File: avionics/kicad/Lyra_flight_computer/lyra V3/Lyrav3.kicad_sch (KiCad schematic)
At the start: 84 parts, among them J1 Screw_Terminal_01x08, J2 Screw_Terminal_01x06, J3 Conn_01x02, J4 Conn_01x02, J5 Conn_01x03, J6 Conn_01x06, J7 USB_B_Micro, J8 Conn_01x04, Q1 AO3401A, Q2 KY6802, Q3 KY6802, U2 BMI088, U3 MPL3115A2, U4 ADXL375BCCZ-RL7, U5 LIS3MDL, U6 ADS1015IDGS, U7 W25Q64JVXGIQ, U8 RP2040, U9 LDK130-33_SOT23_SOT353, X1 S3D12.288000B20F30T

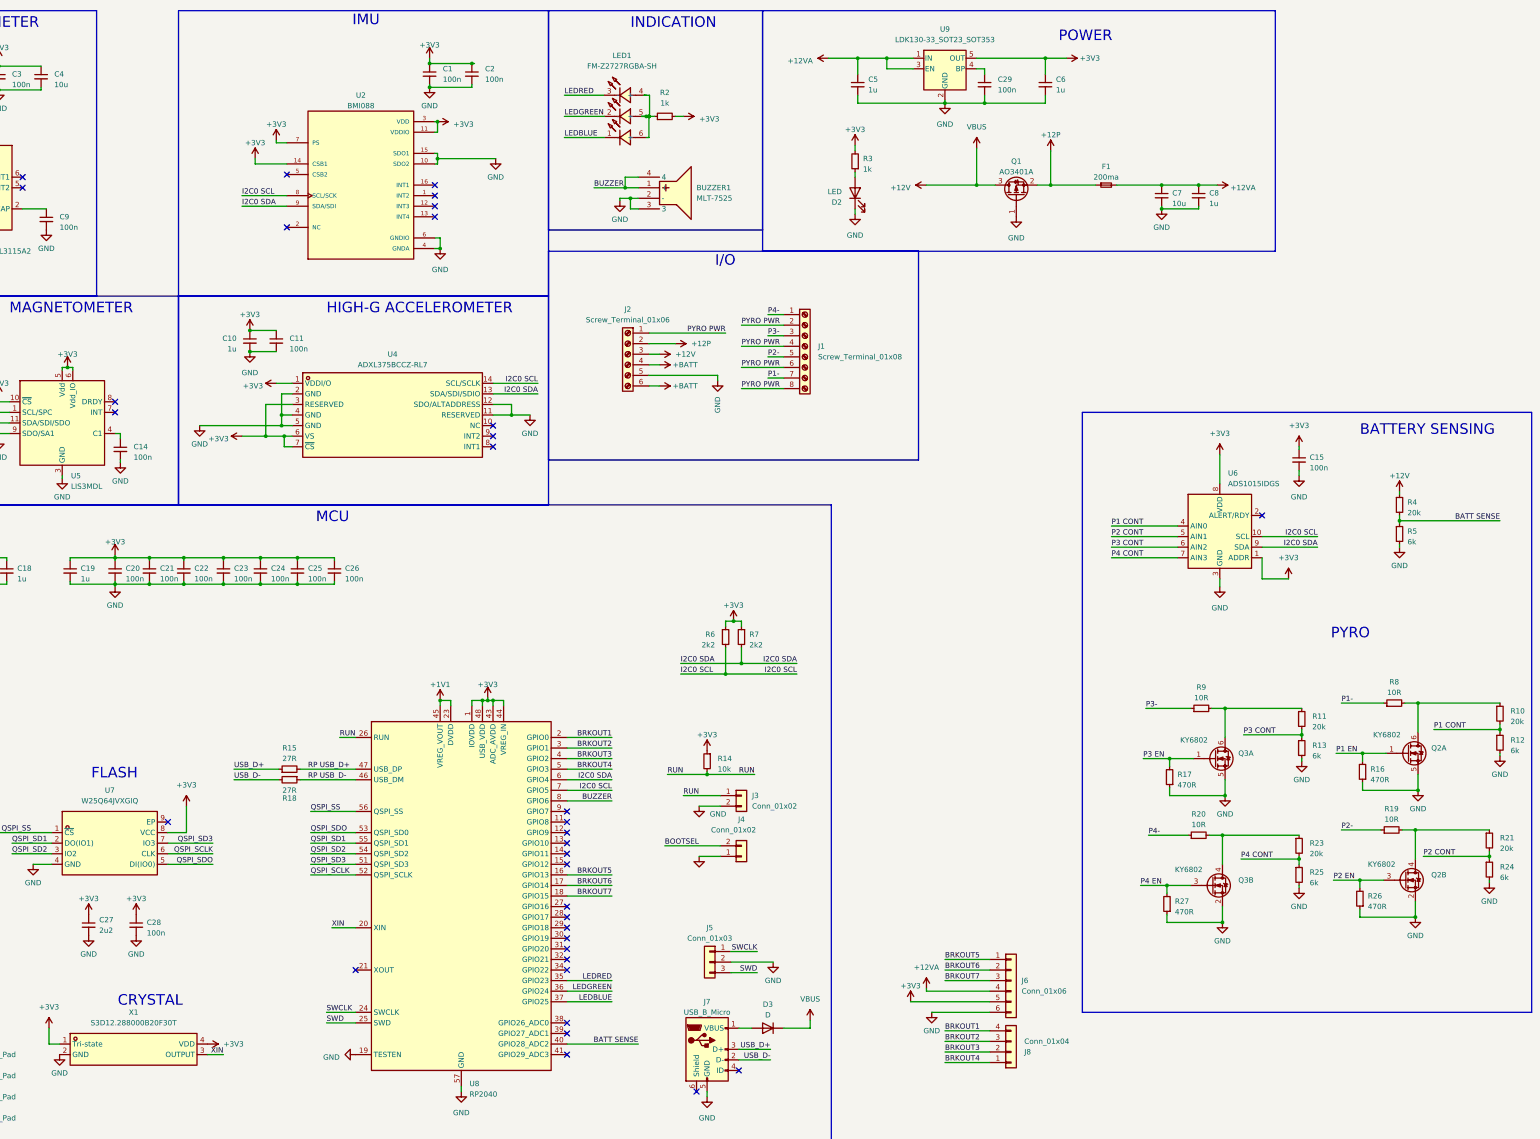
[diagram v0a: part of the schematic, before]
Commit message: more everything to back of board, find JLC components for everything
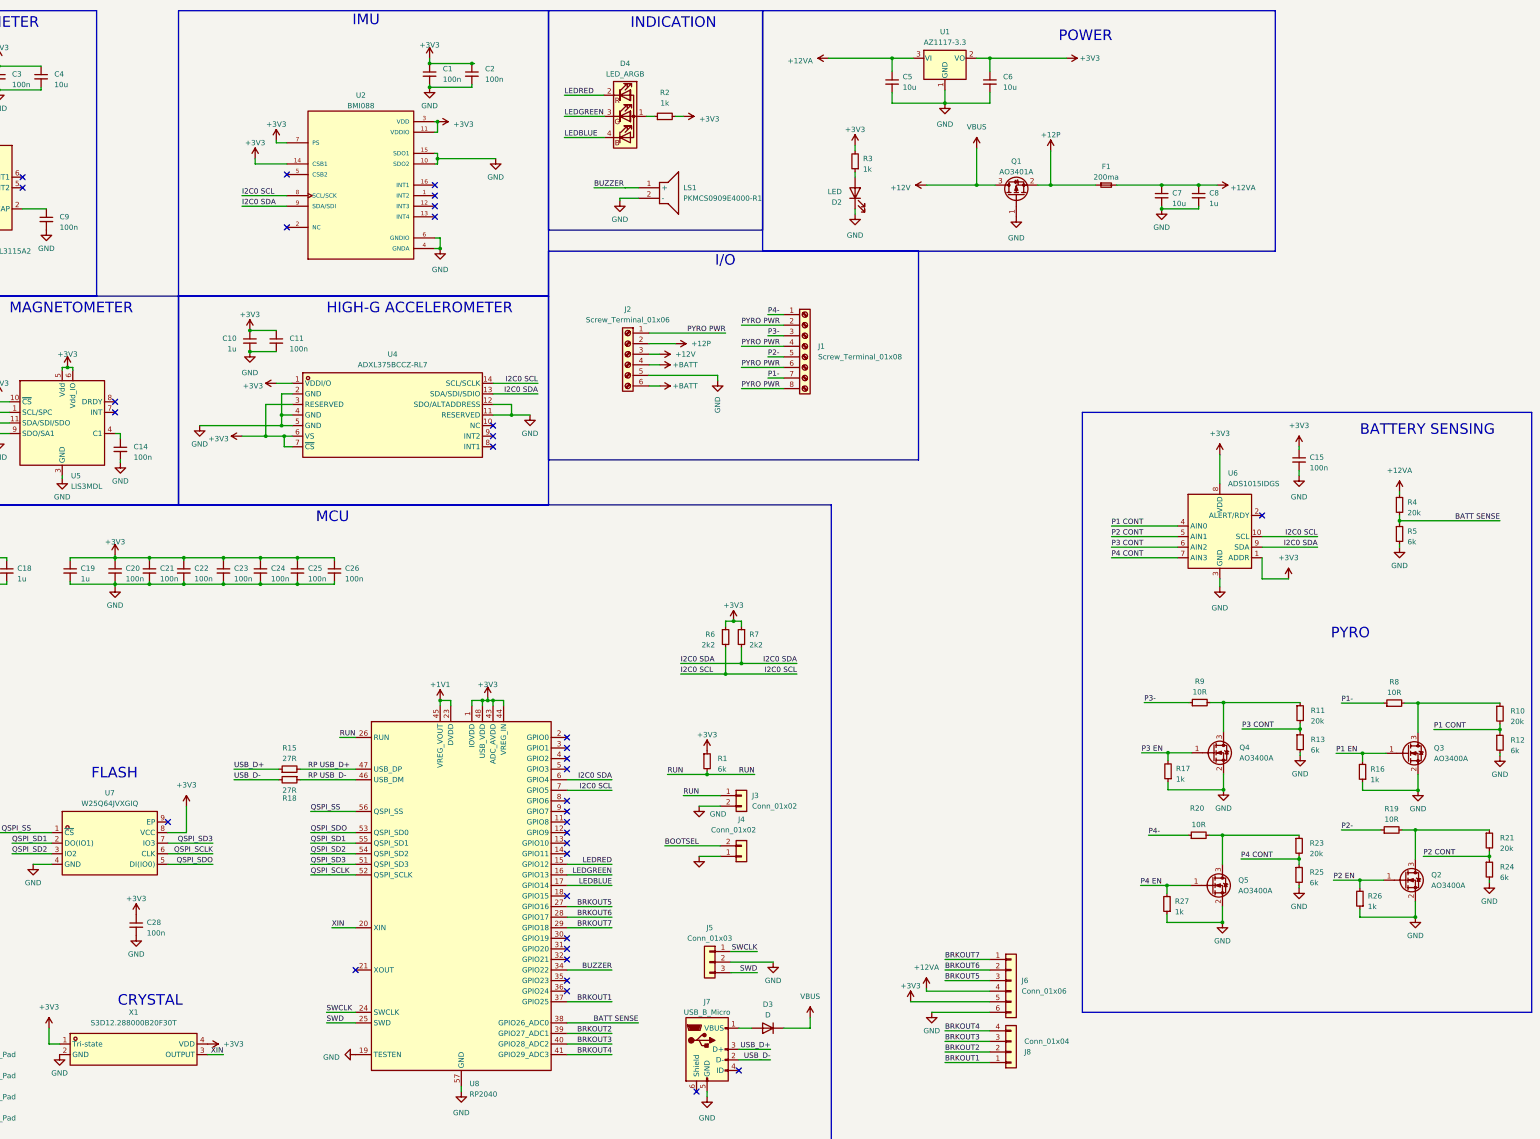
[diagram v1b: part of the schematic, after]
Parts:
- removed BUZZER1: MLT-7525, easyeda2kicad:BUZ-SMD_4P-L7.5-W7.5-P7.59-TL, symbol easyeda2kicad:MLT-7525
- removed C27: 2u2, Capacitor_SMD:C_0402_1005Metric, symbol Device:C_Small
- removed C29: 100n, Capacitor_SMD:C_0402_1005Metric, symbol Device:C_Small
- removed LED1: FM-Z2727RGBA-SH, easyeda2kicad:LED-SMD_6P-L2.7-W2.8-TL, symbol easyeda2kicad:FM-Z2727RGBA-SH
- removed Q2, Q3: KY6802, easyeda2kicad:SOT-23-6_L2.9-W1.6-P0.95-LS2.8-BL, symbol Device:Q_Dual_NMOS_G1S2G2D2S1D1
- removed R14: 10k, Resistor_SMD:R_0402_1005Metric, symbol Device:R_Small
- removed U9: LDK130-33_SOT23_SOT353, easyeda2kicad:SOT-23-5_L3.0-W1.6-P0.95-LS2.8-BL, symbol Regulator_Linear:LDK130-33_SOT23_SOT353
- added D4: LED_ARGB, customfootprints:LED_Cree-PLCC4_2x2mm_CCW, symbol Device:LED_ARGB
- added LS1: PKMCS0909E4000-R1, SamacSys_Parts4:PKMCS0909E4000R1, symbol SamacSys_Parts2:PKMCS0909E4000-R1
- added Q2, Q3, Q4, Q5: AO3400A, Package_TO_SOT_SMD:SOT-23, symbol Transistor_FET:AO3400A
- added R1: 6k, Resistor_SMD:R_0603_1608Metric, symbol Device:R_Small
- added U1: AZ1117-3.3, Package_TO_SOT_SMD:SOT-223, symbol Regulator_Linear:AZ1117-3.3
- C1, C11, C13, C14, C15, C16, C17, C2, C20, C21, C22, C23, C24, C25, C26, C28, C3, C9: footprint Capacitor_SMD:C_0402_1005Metric -> Capacitor_SMD:C_0603_1608Metric; LCSC Part (none) -> C14663
- C10, C12, C18, C19, C8: footprint Capacitor_SMD:C_0402_1005Metric -> Capacitor_SMD:C_0603_1608Metric; LCSC Part (none) -> C15849
- C4, C7: LCSC Part (none) -> C19702
- C5, C6: value 1u -> 10u; footprint Capacitor_SMD:C_0402_1005Metric -> Capacitor_SMD:C_0603_1608Metric; LCSC Part (none) -> C19702
- D2: LCSC Part (none) -> C2297
- D3: footprint Diode_SMD:D_0402_1005Metric -> Diode_SMD:D_SOD-323; LCSC Part (none) -> C2128
- F1: LCSC Part C883104 -> (none); now left out of the parts list
- H1, H2, H3, H4, J1, J2, J3, J6, J8: now left out of the parts list
- Q1: LCSC Part C306862 -> C15127
- R10, R11, R21, R23, R4: footprint Resistor_SMD:R_0402_1005Metric -> Resistor_SMD:R_0603_1608Metric; LCSC Part (none) -> C25804
- R12, R13, R24, R25, R5: footprint Resistor_SMD:R_0402_1005Metric -> Resistor_SMD:R_0603_1608Metric; LCSC Part (none) -> C4260
- R15, R18: footprint Resistor_SMD:R_0402_1005Metric -> Resistor_SMD:R_0603_1608Metric; LCSC Part C2909343 -> C25190
- R16, R17, R26, R27: value 470R -> 1k; footprint Resistor_SMD:R_0402_1005Metric -> Resistor_SMD:R_0603_1608Metric; LCSC Part (none) -> C21190
- R19, R20, R8, R9: footprint Resistor_SMD:R_0402_1005Metric -> Resistor_SMD:R_0603_1608Metric; LCSC Part (none) -> C22859
- R2, R22, R3: footprint Resistor_SMD:R_0402_1005Metric -> Resistor_SMD:R_0603_1608Metric; LCSC Part (none) -> C21190
- R6, R7: footprint Resistor_SMD:R_0402_1005Metric -> Resistor_SMD:R_0603_1608Metric; LCSC Part C163447 -> C4190
- U7: value W25Q64JVXGIQ -> W25Q64JVXGIQ; footprint easyeda2kicad:XSON-8_L4.0-W4.0-P0.80-TL-EP -> Package_SO:SOIC-8_5.23x5.23mm_P1.27mm; LCSC Part C2940195 -> C97521
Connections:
- net +12V: no longer R4.1
- net +12VA: now also R4.1, U1.3 (VI)
- net +3V3: now also R1.1, U1.2 (VO)
- net BATT SENSE : now also U8.38 (GPIO26_ADC0); no longer U8.40 (GPIO28_ADC2)
- net BRKOUT1: now also J8.1 (Pin_1), U8.37 (GPIO25); no longer J8.4 (Pin_4), U8.2 (GPIO0)
- net BRKOUT2: now also J8.2 (Pin_2), U8.39 (GPIO27_ADC1); no longer J8.3 (Pin_3), U8.3 (GPIO1)
- net BRKOUT3: now also J8.3 (Pin_3), U8.40 (GPIO28_ADC2); no longer J8.2 (Pin_2), U8.4 (GPIO2)
- net BRKOUT4: now also J8.4 (Pin_4), U8.41 (GPIO29_ADC3); no longer J8.1 (Pin_1), U8.5 (GPIO3)
- net BRKOUT5: now also J6.3 (Pin_3), U8.27 (GPIO16); no longer J6.1 (Pin_1), U8.16 (GPIO13)
- net BRKOUT6: now also U8.28 (GPIO17); no longer U8.17 (GPIO14)
- net BRKOUT7: now also J6.1 (Pin_1), U8.29 (GPIO18); no longer J6.3 (Pin_3), U8.18 (GPIO15)
- net BUZZER: now also U8.34 (GPIO22), LS1.1 (+); no longer U8.8 (GPIO6)
- net GND: now also LS1.2 (-), Q2.2 (S), Q3.2 (S), Q4.2 (S), Q5.2 (S), U1.1 (GND)
- net LEDBLUE: now also U8.17 (GPIO14), D4.4 (BK); no longer U8.37 (GPIO25)
- net LEDGREEN: now also U8.16 (GPIO13), D4.3 (GK); no longer U8.36 (GPIO24)
- net LEDRED: now also U8.15 (GPIO12), D4.2 (RK); no longer U8.35 (GPIO23)
- net P1 EN : now also Q3.1 (G)
- net P2 EN : now also Q2.1 (G)
- net P3 EN : now also Q4.1 (G)
- net P4 EN : now also Q5.1 (G)
- net RUN: now also R1.2
- net at R19.2, R21.1: now also Q2.3 (D)
- net at R11.1, R9.2: now also Q4.3 (D)
- net at R20.2, R23.1: now also Q5.3 (D)
- net at R10.1, R8.2: now also Q3.3 (D)
- net at R2.1: now also D4.1 (A)
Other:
- moved on the sheet: C5, C6, R11, R13, R17, R9

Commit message: routing init
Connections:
- net BUZZER: now also U8.32 (GPIO21); no longer U8.34 (GPIO22)
- net P1 EN : now also U8.6 (GPIO4)
- net P2 EN : now also U8.7 (GPIO5)
- net P3 EN : now also U8.8 (GPIO6)
- net P4 EN : now also U8.9 (GPIO7)
- net I2C1 SCL: now reaches U8.35 (GPIO23)
- net I2C1 SCL: now also R6.2, U2.8 (SCL/SCK), U3.8 (SCL), U4.14 (SCL/SCLK), U5.1 (SCL/SPC), U6.10 (SCL)
- removed net I2C0 SCL: R6.2, U2.8 (SCL/SCK), U3.8 (SCL), U4.14 (SCL/SCLK), U5.1 (SCL/SPC), U6.10 (SCL), U8.7 (GPIO5)
- net I2C0 SDA renamed I2C1 SDA
- net I2C1 SDA: now also U8.34 (GPIO22); no longer U8.6 (GPIO4)
- no-connect marks 34 -> 30
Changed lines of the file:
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@@
   (junction (at 99.695 94.615) (diameter 0) (color 0 0 0 0)
   )
-  (no_connect (at 175.895 202.565))
   (no_connect (at 80.01 207.645))
   (no_connect (at 144.145 57.15))
+  (no_connect (at 175.895 194.945))
   (no_connect (at 175.895 248.285))
+  (no_connect (at 175.895 189.865))
   (no_connect (at 175.895 215.265))
   (no_connect (at 175.895 238.125))
   (no_connect (at 108.585 64.77))
   (no_connect (at 45.085 55.245))
-  (no_connect (at 175.895 240.665))
   (no_connect (at 207.01 272.415))
   (no_connect (at 217.17 267.335))
@@
   (no_connect (at 175.895 212.725))
   (no_connect (at 67.31 106.68))
-  (no_connect (at 175.895 245.745))
   (no_connect (at 158.115 112.395))
-  (no_connect (at 175.895 205.105))
   (no_connect (at 45.085 52.705))
   (no_connect (at 175.895 225.425))
   (no_connect (at 144.145 59.69))
-  (no_connect (at 175.895 189.865))
-  (no_connect (at 175.895 194.945))
+  (no_connect (at 175.895 187.325))
   (no_connect (at 144.145 62.23))
   (no_connect (at 158.115 114.935))
-  (no_connect (at 175.895 187.325))
   (no_connect (at 175.895 207.645))
   (wire (pts (xy 106.045 102.235) (xy 109.855 102.235))
@@
     (stroke (width 0) (type default))
   )
-  (wire (pts (xy 175.895 197.485) (xy 186.69 197.485))
-    (stroke (width 0) (type default))
-  )
   (wire (pts (xy 277.495 260.35) (xy 266.7 260.35))
     (stroke (width 0) (type default))
@@
     (stroke (width 0) (type default))
   )
+  (wire (pts (xy 182.245 202.565) (xy 175.895 202.565))
+    (stroke (width 0) (type default))
+  )
   (wire (pts (xy 306.705 139.065) (xy 322.58 139.065))
     (stroke (width 0) (type default))
@@
     (stroke (width 0) (type default))
   )
-  (wire (pts (xy 175.895 200.025) (xy 186.69 200.025))
+  (wire (pts (xy 175.895 245.745) (xy 186.69 245.745))
     (stroke (width 0) (type default))
   )
@@
     (stroke (width 0) (type default))
   )
+  (wire (pts (xy 175.895 243.205) (xy 186.69 243.205))
+    (stroke (width 0) (type default))
+  )
   (wire (pts (xy 120.015 144.145) (xy 120.015 144.78))
     (stroke (width 0) (type default))
@@
     (stroke (width 0) (type default))
   )
+  (wire (pts (xy 182.245 200.025) (xy 175.895 200.025))
+    (stroke (width 0) (type default))
+  )
   (wire (pts (xy 23.495 150.495) (xy 32.385 150.495))
     (stroke (width 0) (type default))
@@
     (stroke (width 0) (type default))
   )
+  (wire (pts (xy 182.245 205.105) (xy 175.895 205.105))
+    (stroke (width 0) (type default))
+  )
   (wire (pts (xy 158.115 102.235) (xy 168.91 102.235))
     (stroke (width 0) (type default))
@@
     (stroke (width 0) (type default))
   )
+  (wire (pts (xy 182.245 197.485) (xy 175.895 197.485))
+    (stroke (width 0) (type default))
+  )
   (wire (pts (xy 114.3 215.265) (xy 125.095 215.265))
     (stroke (width 0) (type default))
@@
     (stroke (width 0) (type default))
   )
-  (wire (pts (xy 175.895 243.205) (xy 186.69 243.205))
+  (wire (pts (xy 175.895 240.665) (xy 186.69 240.665))
     (stroke (width 0) (type default))
   )
@@
     (effects (font (size 2.54 2.54)) (justify left bottom))
   )
-  (label "I2C0 SCL" (at 203.2 172.085 0) (fields_autoplaced)
+  (label "I2C1 SCL" (at 203.2 172.085 0) (fields_autoplaced)
     (effects (font (size 1.27 1.27)) (justify left bottom))
   )
@@
     (effects (font (size 1.27 1.27)) (justify right bottom))
   )
-  (label "I2C0 SDA" (at 97.79 59.69 0) (fields_autoplaced)
+  (label "I2C1 SDA" (at 97.79 59.69 0) (fields_autoplaced)
     (effects (font (size 1.27 1.27)) (justify left bottom))
   )
@@
     (effects (font (size 1.27 1.27)) (justify right bottom))
   )
-  (label "I2C0 SDA" (at 168.91 104.775 180) (fields_autoplaced)
-    (effects (font (size 1.27 1.27)) (justify right bottom))
-  )
-  (label "I2C0 SDA" (at 31.115 111.76 0) (fields_autoplaced)
+  (label "I2C1 SDA" (at 168.91 104.775 180) (fields_autoplaced)
+    (effects (font (size 1.27 1.27)) (justify right bottom))
+  )
+  (label "I2C1 SDA" (at 31.115 111.76 0) (fields_autoplaced)
     (effects (font (size 1.27 1.27)) (justify left bottom))
   )
@@
     (effects (font (size 1.27 1.27)) (justify left bottom))
   )
-  (label "BUZZER" (at 186.69 243.205 180) (fields_autoplaced)
+  (label "BUZZER" (at 186.69 240.665 180) (fields_autoplaced)
     (effects (font (size 1.27 1.27)) (justify right bottom))
   )
@@
     (effects (font (size 1.27 1.27)) (justify left bottom))
   )
-  (label "I2C0 SDA" (at 13.97 52.705 0) (fields_autoplaced)
+  (label "I2C1 SDA" (at 13.97 52.705 0) (fields_autoplaced)
     (effects (font (size 1.27 1.27)) (justify left bottom))
   )
@@
     (effects (font (size 1.27 1.27)) (justify left bottom))
   )
+  (label "P1 EN " (at 182.245 197.485 180) (fields_autoplaced)
+    (effects (font (size 1.27 1.27)) (justify right bottom))
+  )
   (label "BRKOUT6" (at 266.7 243.205 0) (fields_autoplaced)
     (effects (font (size 1.27 1.27)) (justify left bottom))
   )
-  (label "I2C0 SCL" (at 168.91 102.235 180) (fields_autoplaced)
+  (label "I2C1 SCL" (at 168.91 102.235 180) (fields_autoplaced)
     (effects (font (size 1.27 1.27)) (justify right bottom))
   )
@@
     (effects (font (size 1.27 1.27)) (justify right bottom))
   )
-  (label "I2C0 SCL" (at 186.69 200.025 180) (fields_autoplaced)
+  (label "I2C1 SCL" (at 186.69 245.745 180) (fields_autoplaced)
     (effects (font (size 1.27 1.27)) (justify right bottom))
   )
@@
     (effects (font (size 1.27 1.27)) (justify left bottom))
   )
-  (label "I2C0 SDA" (at 231.14 169.545 180) (fields_autoplaced)
+  (label "I2C1 SDA" (at 231.14 169.545 180) (fields_autoplaced)
     (effects (font (size 1.27 1.27)) (justify right bottom))
   )
@@
     (effects (font (size 1.27 1.27)) (justify right bottom))
   )
+  (label "P2 EN " (at 182.245 200.025 180) (fields_autoplaced)
+    (effects (font (size 1.27 1.27)) (justify right bottom))
+  )
   (label "LEDRED" (at 186.69 217.805 180) (fields_autoplaced)
     (effects (font (size 1.27 1.27)) (justify right bottom))
@@
     (effects (font (size 1.27 1.27)) (justify left bottom))
   )
-  (label "I2C0 SCL" (at 31.115 109.22 0) (fields_autoplaced)
-    (effects (font (size 1.27 1.27)) (justify left bottom))
-  )
-  (label "I2C0 SCL" (at 97.79 57.15 0) (fields_autoplaced)
+  (label "I2C1 SCL" (at 31.115 109.22 0) (fields_autoplaced)
+    (effects (font (size 1.27 1.27)) (justify left bottom))
+  )
+  (label "I2C1 SCL" (at 97.79 57.15 0) (fields_autoplaced)
     (effects (font (size 1.27 1.27)) (justify left bottom))
   )
@@
     (effects (font (size 1.27 1.27)) (justify left bottom))
   )
-  (label "I2C0 SCL" (at 231.14 172.085 180) (fields_autoplaced)
+  (label "I2C1 SCL" (at 231.14 172.085 180) (fields_autoplaced)
     (effects (font (size 1.27 1.27)) (justify right bottom))
   )
@@
     (effects (font (size 1.27 1.27)) (justify left bottom))
   )
-  (label "I2C0 SDA" (at 356.235 141.605 180) (fields_autoplaced)
+  (label "I2C1 SDA" (at 356.235 141.605 180) (fields_autoplaced)
     (effects (font (size 1.27 1.27)) (justify right bottom))
   )
@@
     (effects (font (size 1.27 1.27)) (justify left bottom))
   )
-  (label "I2C0 SDA" (at 186.69 197.485 180) (fields_autoplaced)
+  (label "I2C1 SDA" (at 186.69 243.205 180) (fields_autoplaced)
     (effects (font (size 1.27 1.27)) (justify right bottom))
   )
@@
     (effects (font (size 1.27 1.27)) (justify right bottom))
   )
+  (label "P4 EN " (at 182.245 205.105 180) (fields_autoplaced)
+    (effects (font (size 1.27 1.27)) (justify right bottom))
+  )
   (label "BRKOUT1" (at 186.69 250.825 180) (fields_autoplaced)
     (effects (font (size 1.27 1.27)) (justify right bottom))
@@
     (effects (font (size 1.27 1.27)) (justify left bottom))
   )
-  (label "I2C0 SCL" (at 13.97 55.245 0) (fields_autoplaced)
+  (label "I2C1 SCL" (at 13.97 55.245 0) (fields_autoplaced)
     (effects (font (size 1.27 1.27)) (justify left bottom))
   )
@@
     (effects (font (size 1.27 1.27)) (justify left bottom))
   )
-  (label "I2C0 SDA" (at 203.2 169.545 0) (fields_autoplaced)
+  (label "I2C1 SDA" (at 203.2 169.545 0) (fields_autoplaced)
     (effects (font (size 1.27 1.27)) (justify left bottom))
   )
@@
     (effects (font (size 1.27 1.27)) (justify left bottom))
   )
+  (label "P3 EN " (at 182.245 202.565 180) (fields_autoplaced)
+    (effects (font (size 1.27 1.27)) (justify right bottom))
+  )
   (label "QSPI_SS" (at 114.3 205.105 0) (fields_autoplaced)
     (effects (font (size 1.27 1.27)) (justify left bottom))
@@
     (effects (font (size 1.27 1.27)) (justify left bottom))
   )
-  (label "I2C0 SCL" (at 356.235 139.065 180) (fields_autoplaced)
-    (effects (font (size 1.27 1.27)) (justify right bottom))
-  )
+  (label "I2C1 SCL" (at 356.235 139.065 180) (fields_autoplaced)
+    (effects (font (size 1.27 1.27)) (justify right bottom))
+  )
